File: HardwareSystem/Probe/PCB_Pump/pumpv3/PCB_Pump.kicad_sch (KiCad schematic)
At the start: 23 parts, among them J1 Conn_01x04_Pin, Q1 IRF510, Q2 IRF4905, U2 MC33063AP, U3 LM7805_TO220

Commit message: updates on both boards
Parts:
- added J2: Conn_01x04_Pin, Connector_PinHeader_2.54mm:PinHeader_1x04_P2.54mm_Vertical, symbol Connector:Conn_01x04_Pin
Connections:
- net +5V: now also J2.4 (Pin_4)
- net GND: now also J2.1 (Pin_1)
- net SDA: now reaches A2.A4 (A4/SDA)
- net SDA: now also J2.2 (Pin_2)
- net SCL: now reaches A2.A5 (A5/SCL)
- net SCL: now also J2.3 (Pin_3)
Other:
- note added: "Battery Level"
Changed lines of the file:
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@@
+    (fill (type none))
+  )
+  (rectangle (start 175.26 99.06) (end 196.85 114.3)
+    (stroke (width 0) (type default))
     (fill (type none))
   )
@@
   )
   (text "Battery Charging Module" (at 87.63 78.74 0)
+    (effects (font (size 1.27 1.27)) (justify left bottom))
+  )
+  (text "Battery Level" (at 175.26 97.79 0)
     (effects (font (size 1.27 1.27)) (justify left bottom))
   )
@@
     )
   )
+  (global_label "SCL" (shape input) (at 189.23 110.49 0) (fields_autoplaced)
+    (effects (font (size 1.27 1.27)) (justify left))
+    (property "Intersheetrefs" "${INTERSHEET_REFS}" (at 195.7228 110.49 0)
+      (effects (font (size 1.27 1.27)) (justify left) hide)
+    )
+  )
   (global_label "3V7-" (shape input) (at 146.05 45.72 180) (fields_autoplaced)
     (effects (font (size 1.27 1.27)) (justify right))
@@
     )
   )
+  (global_label "SCL" (shape input) (at 26.67 57.15 180) (fields_autoplaced)
+    (effects (font (size 1.27 1.27)) (justify right))
+    (property "Intersheetrefs" "${INTERSHEET_REFS}" (at 20.1772 57.15 0)
+      (effects (font (size 1.27 1.27)) (justify right) hide)
+    )
+  )
   (global_label "Echo" (shape input) (at 189.23 87.63 0) (fields_autoplaced)
     (effects (font (size 1.27 1.27)) (justify left))
@@
     (effects (font (size 1.27 1.27)) (justify left))
     (property "Intersheetrefs" "${INTERSHEET_REFS}" (at 178.1847 45.72 0)
+      (effects (font (size 1.27 1.27)) (justify left) hide)
+    )
+  )
+  (global_label "SDA" (shape input) (at 26.67 59.69 180) (fields_autoplaced)
+    (effects (font (size 1.27 1.27)) (justify right))
+    (property "Intersheetrefs" "${INTERSHEET_REFS}" (at 20.1167 59.69 0)
+      (effects (font (size 1.27 1.27)) (justify right) hide)
+    )
+  )
+  (global_label "SDA" (shape input) (at 189.23 107.95 0) (fields_autoplaced)
+    (effects (font (size 1.27 1.27)) (justify left))
+    (property "Intersheetrefs" "${INTERSHEET_REFS}" (at 195.7833 107.95 0)
       (effects (font (size 1.27 1.27)) (justify left) hide)
     )
@@
         (path "/57512134-c0e5-4e7f-86c3-2738c5b8ae18"
           (reference "C2") (unit 1)
+        )
+      )
+    )
+  )
+  (symbol (lib_id "Connector:Conn_01x04_Pin") (at 184.15 107.95 0) (unit 1)
+    (in_bom yes) (on_board yes) (dnp no) (fields_autoplaced)
+    (property "Reference" "J2" (at 184.785 100.33 0)
+      (effects (font (size 1.27 1.27)))
+    )
+    (property "Value" "Conn_01x04_Pin" (at 184.785 102.87 0)
+      (effects (font (size 1.27 1.27)))
+    )
+    (property "Footprint" "Connector_PinHeader_2.54mm:PinHeader_1x04_P2.54mm_Vertical" (at 184.15 107.95 0)
+      (effects (font (size 1.27 1.27)) hide)
+    )
+    (property "Datasheet" "~" (at 184.15 107.95 0)
+      (effects (font (size 1.27 1.27)) hide)
+    )
+    (pin "1")
+    (pin "2")
+    (pin "3")
+    (pin "4")
+    (instances
+      (project "PCB_Pump"
+        (path "/57512134-c0e5-4e7f-86c3-2738c5b8ae18"
+          (reference "J2") (unit 1)
         )
       )
@@
     )
   )
+  (symbol (lib_id "power:+5V") (at 189.23 113.03 270) (unit 1)
+    (in_bom yes) (on_board yes) (dnp no) (fields_autoplaced)
+    (property "Reference" "#PWR011" (at 185.42 113.03 0)
+      (effects (font (size 1.27 1.27)) hide)
+    )
+    (property "Value" "+5V" (at 193.04 113.03 90)
+      (effects (font (size 1.27 1.27)) (justify left))
+    )
+    (property "Footprint" "" (at 189.23 113.03 0)
+      (effects (font (size 1.27 1.27)) hide)
+    )
+    (property "Datasheet" "" (at 189.23 113.03 0)
+      (effects (font (size 1.27 1.27)) hide)
+    )
+    (pin "1")
+    (instances
+      (project "PCB_Pump"
+        (path "/57512134-c0e5-4e7f-86c3-2738c5b8ae18"
+          (reference "#PWR011") (unit 1)
+        )
+      )
+    )
+  )
   (symbol (lib_id "Diode:1N5819") (at 201.93 26.67 180) (unit 1)
     (in_bom yes) (on_board yes) (dnp no)
@@
         )
       )
+    )
+  )
+  (symbol (lib_id "power:GND") (at 189.23 105.41 90) (unit 1)
+    (in_bom yes) (on_board yes) (dnp no) (fields_autoplaced)
+    (property "Reference" "#PWR012" (at 195.58 105.41 0)
+      (effects (font (size 1.27 1.27)) hide)
+    )
+    (property "Value" "GND" (at 193.04 105.41 90)
+      (effects (font (size 1.27 1.27)) (justify right))
+    )
+    (property "Footprint" "" (at 189.23 105.41 0)
+      (effects (font (size 1.27 1.27)) hide)
+    )
+    (property "Datasheet" "" (at 189.23 105.41 0)
+      (effects (font (size 1.27 1.27)) hide)
+    )
+    (pin "1")
+    (instances
+      (project "PCB_Pump"
+        (path "/57512134-c0e5-4e7f-86c3-2738c5b8ae18"
+          (reference "#PWR012") (unit 1)
+        )
+      )

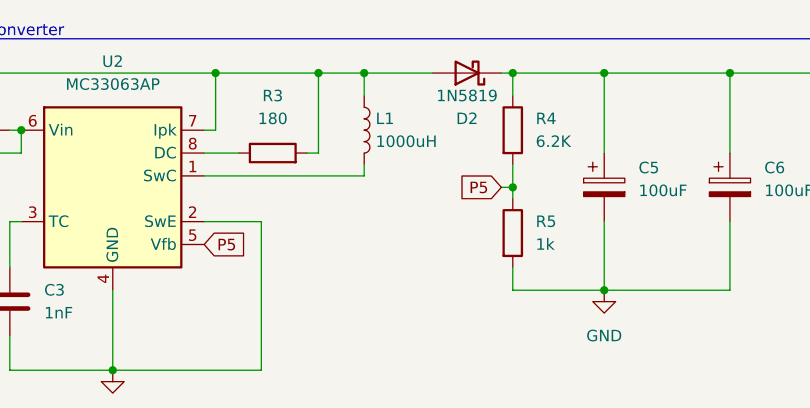
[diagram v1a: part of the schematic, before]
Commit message: changed buck wiring
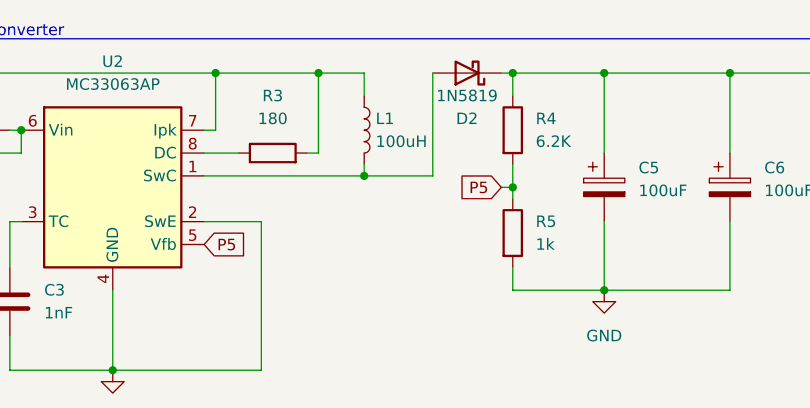
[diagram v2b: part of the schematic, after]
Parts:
- L1: value 1000uH -> 100uH
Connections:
- net at L1.1, R2.1, R3.2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: no longer D2.2 (A)
- net at L1.2, U2.1 (SwC): now also D2.2 (A)
